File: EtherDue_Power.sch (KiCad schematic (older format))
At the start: 48 parts, among them Q501 BC847BSMD, U303 LMV358IDGKR, U501 POWERJACK, U502 LM2734Y, U503 FDN340P, U504 FDN340P, U505 NCP1117ST33T3G

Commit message: Final ERC cleanup, export net file
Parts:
- R503: renamed from 10K501; value R -> 10K
- renumbered R503 to R504, R504 to R505, U303 to U203
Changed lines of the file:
@@
-EESchema Schematic File Version 2  date Thu 11 Apr 2013 15:52:58 EST
+EESchema Schematic File Version 2  date Thu 11 Apr 2013 16:32:55 EST
 LIBS:power
 LIBS:device
@@
 $EndComp
 $Comp
-L LM358 U303
+L LM358 U203
 U 2 1 515CD980
 P 5300 4700
-F 0 "U303" H 5250 4900 60  0000 L CNN
+F 0 "U203" H 5250 4900 60  0000 L CNN
 F 1 "LMV358IDGKR" H 5250 4450 60  0000 L CNN
 F 2 "" H 5300 4700 60  0001 C CNN
@@
 $EndComp
 $Comp
-L R R504
+L R R505
 U 1 1 515CD3C9
 P 6250 3000
-F 0 "R504" V 6330 3000 50  0000 C CNN
+F 0 "R505" V 6330 3000 50  0000 C CNN
 F 1 "10K" V 6250 3000 50  0000 C CNN
 F 2 "" H 6250 3000 60  0001 C CNN
@@
 $EndComp
 $Comp
-L R R503
+L R R504
 U 1 1 515CD3B6
 P 6250 2350
-F 0 "R503" V 6330 2350 50  0000 C CNN
+F 0 "R504" V 6330 2350 50  0000 C CNN
 F 1 "52K3" V 6250 2350 50  0000 C CNN
 F 2 "" H 6250 2350 60  0001 C CNN
@@
 $EndComp
 $Comp
-L R 10K501
+L R R503
 U 1 1 515CCC34
 P 4150 1650
-F 0 "10K501" V 4230 1650 50  0000 C CNN
-F 1 "R" V 4150 1650 50  0000 C CNN
+F 0 "R503" V 4230 1650 50  0000 C CNN
+F 1 "10K" V 4150 1650 50  0000 C CNN
 F 2 "" H 4150 1650 60  0001 C CNN
 F 3 "" H 4150 1650 60  0001 C CNN
@@
 	1    0    0    -1
 $EndComp
+$Comp
+L PWR_FLAG #FLG078
+U 1 1 51666680
+P 2150 1900
+F 0 "#FLG078" H 2150 1995 30  0001 C CNN
+F 1 "PWR_FLAG" H 2150 2080 30  0000 C CNN
+F 2 "" H 2150 1900 60  0000 C CNN
+F 3 "" H 2150 1900 60  0000 C CNN
+	1    2150 1900
+	1    0    0    -1
+$EndComp
+Connection ~ 2150 1900
 $EndSCHEMATC

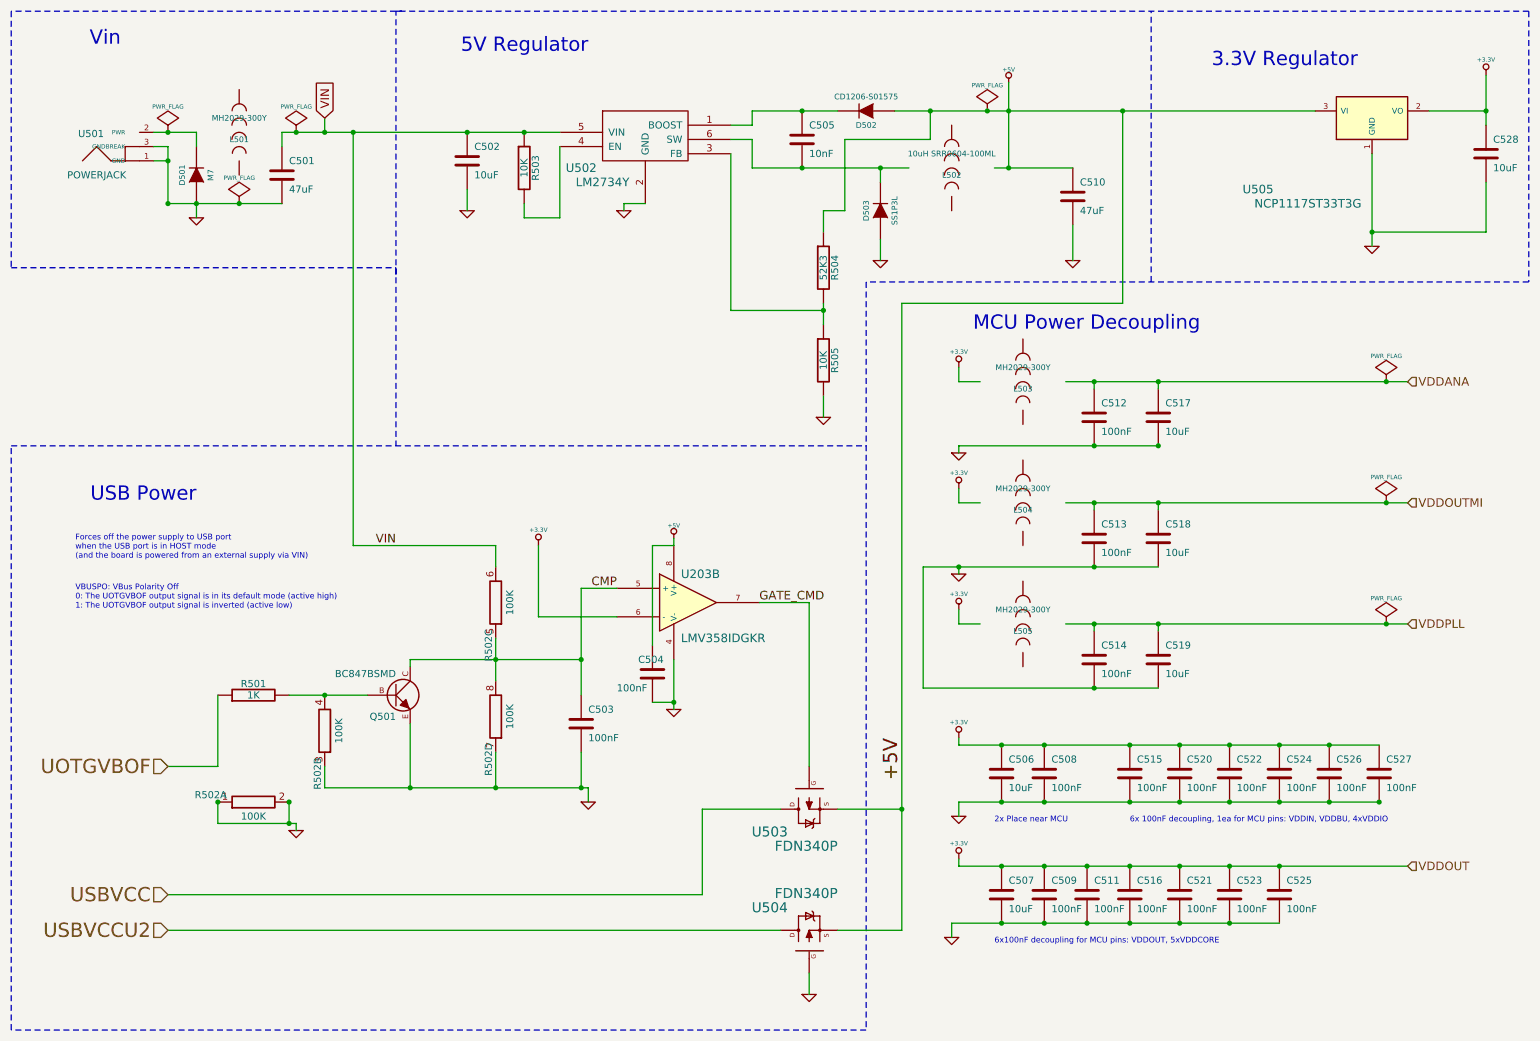
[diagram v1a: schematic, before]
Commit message: Edit pass of footprints, cleanup symbols, etc.
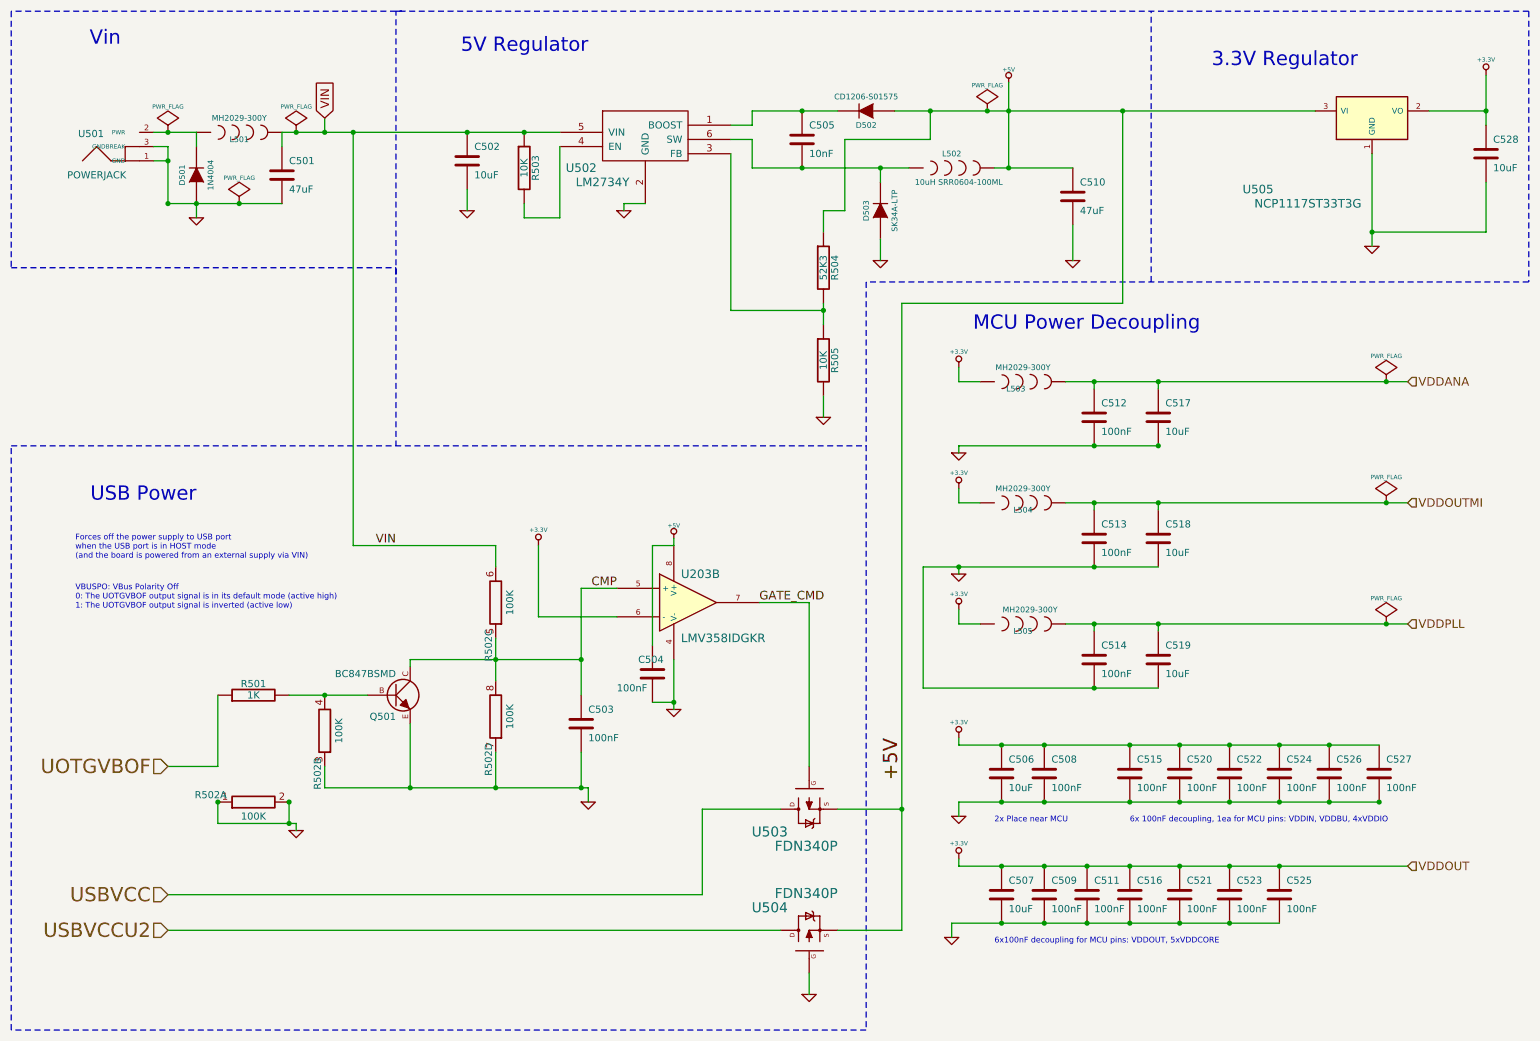
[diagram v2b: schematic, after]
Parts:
- D501: value M7 -> 1N4004
- D503: value SS1P3L -> SK34A-LTP
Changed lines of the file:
@@
-EESchema Schematic File Version 2  date Thu 11 Apr 2013 16:32:55 EST
+EESchema Schematic File Version 2  date Fri 03 May 2013 15:34:29 EST
+LIBS:freetronics_kicad_sch_lib
 LIBS:power
 LIBS:device
@@
 LIBS:contrib
 LIBS:valves
-LIBS:freetronics_kicad_sch_lib
 LIBS:EtherDue-cache
 EELAYER 24 0
@@
 Sheet 5 6
 Title ""
-Date "11 apr 2013"
+Date "3 may 2013"
 Rev ""
 Comp ""
@@
 U 1 1 515D021D
 P 7650 4850
-F 0 "L505" V 7600 4850 40  0000 C CNN
-F 1 "MH2029-300Y" V 7750 4850 40  0000 C CNN
+F 0 "L505" H 7650 4800 40  0000 C CNN
+F 1 "MH2029-300Y" H 7700 4950 40  0000 C CNN
 F 2 "" H 7650 4850 60  0001 C CNN
 F 3 "" H 7650 4850 60  0001 C CNN
 	1    7650 4850
-	0    -1   -1   0
+	1    0    0    -1
 $EndComp
 $Comp
@@
 U 1 1 515CFE4F
 P 7650 4000
-F 0 "L504" V 7600 4000 40  0000 C CNN
-F 1 "MH2029-300Y" V 7750 4000 40  0000 C CNN
+F 0 "L504" H 7650 3950 40  0000 C CNN
+F 1 "MH2029-300Y" H 7650 4100 40  0000 C CNN
 F 2 "" H 7650 4000 60  0001 C CNN
 F 3 "" H 7650 4000 60  0001 C CNN
 	1    7650 4000
-	0    -1   -1   0
+	1    0    0    -1
 $EndComp
 $Comp
@@
 U 1 1 515CFDAA
 P 7650 3150
-F 0 "L503" V 7600 3150 40  0000 C CNN
-F 1 "MH2029-300Y" V 7750 3150 40  0000 C CNN
+F 0 "L503" H 7600 3100 40  0000 C CNN
+F 1 "MH2029-300Y" H 7650 3250 40  0000 C CNN
 F 2 "" H 7650 3150 60  0001 C CNN
 F 3 "" H 7650 3150 60  0001 C CNN
 	1    7650 3150
-	0    -1   -1   0
+	1    0    0    -1
 $EndComp
 $Comp
@@
 P 6650 1950
 F 0 "D503" H 6650 2050 40  0000 C CNN
-F 1 "SS1P3L" H 6650 1850 40  0000 C CNN
+F 1 "SK34A-LTP" H 6650 1850 40  0000 C CNN
 F 2 "" H 6650 1950 60  0001 C CNN
 F 3 "" H 6650 1950 60  0001 C CNN
@@
 U 1 1 515CD388
 P 7150 1650
-F 0 "L502" V 7100 1650 40  0000 C CNN
-F 1 "10uH SRR0604-100ML" V 7250 1650 40  0000 C CNN
+F 0 "L502" H 7150 1750 40  0000 C CNN
+F 1 "10uH SRR0604-100ML" H 7200 1550 40  0000 C CNN
 F 2 "" H 7150 1650 60  0001 C CNN
 F 3 "" H 7150 1650 60  0001 C CNN
 	1    7150 1650
-	0    -1   -1   0
+	1    0    0    -1
 $EndComp
 $Comp
@@
 P 1850 1700
 F 0 "D501" H 1850 1800 40  0000 C CNN
-F 1 "M7" H 1850 1600 40  0000 C CNN
+F 1 "1N4004" H 1850 1600 40  0000 C CNN
 F 2 "" H 1850 1700 60  0001 C CNN
 F 3 "" H 1850 1700 60  0001 C CNN
@@
 U 1 1 515CCB10
 P 2150 1400
-F 0 "L501" V 2100 1400 40  0000 C CNN
-F 1 "MH2029-300Y" V 2250 1400 40  0000 C CNN
+F 0 "L501" H 2150 1350 40  0000 C CNN
+F 1 "MH2029-300Y" H 2150 1500 40  0000 C CNN
 F 2 "" H 2150 1400 60  0001 C CNN
 F 3 "" H 2150 1400 60  0001 C CNN
 	1    2150 1400
-	0    -1   -1   0
-$EndComp
-$Comp
+	1    0    0    -1
+$EndComp
+$Comp

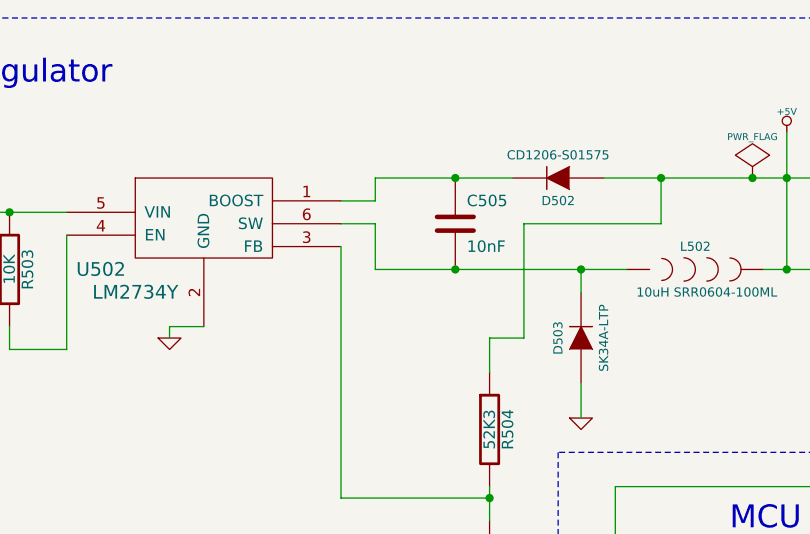
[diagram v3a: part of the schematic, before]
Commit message: Footprints checked, components imported to board but most not placed
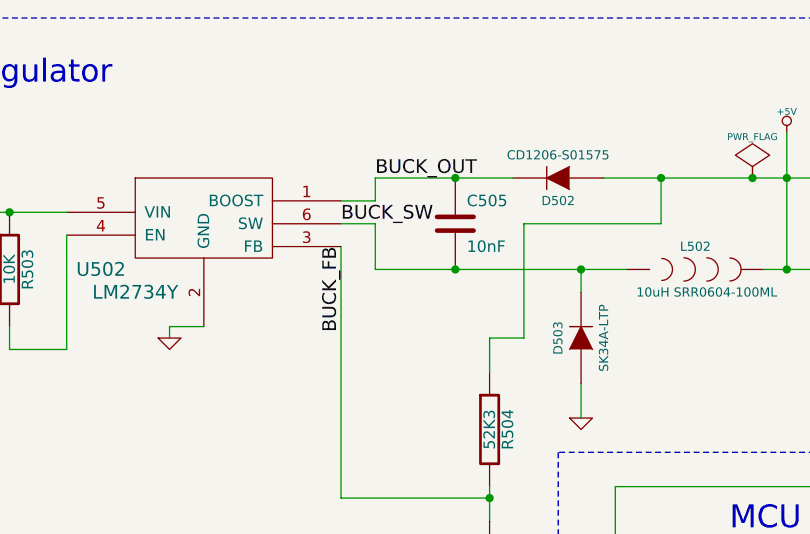
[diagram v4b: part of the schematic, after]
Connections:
- net BUCK_OUT: now reaches C505.1, D502.K, U502.1 (BOOST)
- net BUCK_FB: now reaches R504.2, R505.1, U502.3 (FB)
- net BUCK_SW: now reaches C505.2, D503.K, L502.1, U502.6 (SW)
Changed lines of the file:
@@
-EESchema Schematic File Version 2  date Tue 04 Jun 2013 15:53:49 EST
+EESchema Schematic File Version 2  date Thu 06 Jun 2013 09:35:07 EST
 LIBS:freetronics_kicad_sch_lib
 LIBS:power
@@
 Sheet 5 6
 Title ""
-Date "4 jun 2013"
+Date "5 jun 2013"
 Rev ""
 Comp ""
@@
 $EndComp
 Connection ~ 2150 1900
+Text Label 5600 1550 3    60   ~ 0
+BUCK_FB
+Text Label 5750 1250 0    60   ~ 0
+BUCK_OUT
+Text Label 5600 1450 0    60   ~ 0
+BUCK_SW
 $EndSCHEMATC

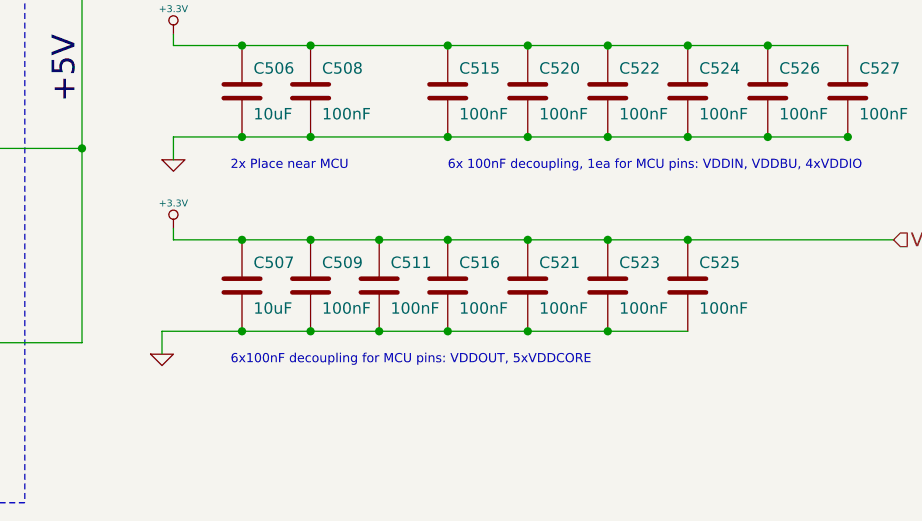
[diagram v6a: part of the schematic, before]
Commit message: All modules placed roughly on PCB
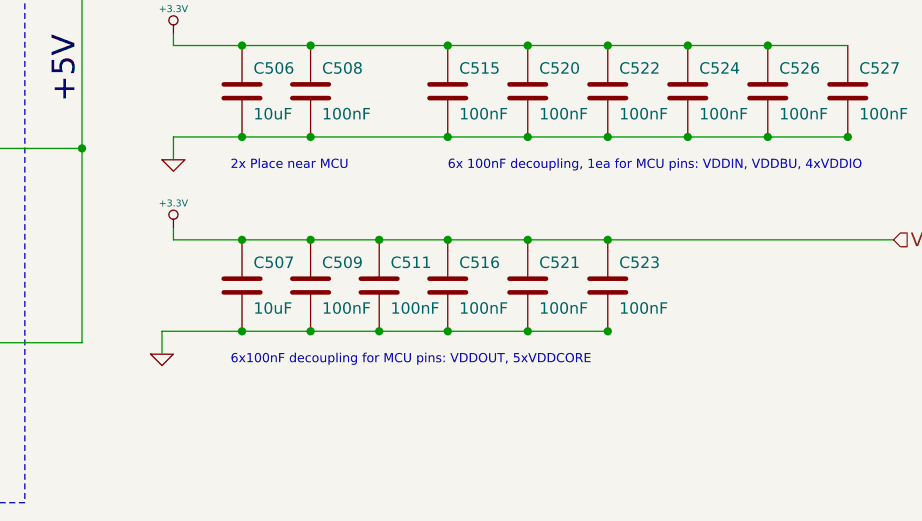
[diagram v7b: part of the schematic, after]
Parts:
- removed C525: 100nF, symbol C
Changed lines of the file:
@@
-EESchema Schematic File Version 2  date Thu 06 Jun 2013 10:26:06 EST
+EESchema Schematic File Version 2  date Thu 06 Jun 2013 15:43:54 EST
 LIBS:freetronics_kicad_sch_lib
 LIBS:power
@@
 Wire Wire Line
 	7150 7050 7150 6950
-Wire Wire Line
-	7150 6950 9450 6950
 Connection ~ 7200 4450
 Wire Wire Line
@@
 Connection ~ 7800 6550
 Connection ~ 8750 6550
-Connection ~ 9450 6550
 Connection ~ 7500 6950
 Connection ~ 8400 6950
@@
 	1    0    0    -1
 $EndComp
-$Comp
-L C C525
-U 1 1 515CFFBF
-P 9450 6750
-F 0 "C525" H 9500 6850 50  0000 L CNN
-F 1 "100nF" H 9500 6650 50  0000 L CNN
-F 2 "" H 9450 6750 60  0001 C CNN
-F 3 "" H 9450 6750 60  0001 C CNN
-	1    9450 6750
-	1    0    0    -1
-$EndComp
 Text Notes 7450 7100 0    40   ~ 0
 6x100nF decoupling for MCU pins: VDDOUT, 5xVDDCORE
@@
 Text Label 5600 1450 0    60   ~ 0
 BUCK_SW
+Wire Wire Line
+	7150 6950 9100 6950
 $EndSCHEMATC
